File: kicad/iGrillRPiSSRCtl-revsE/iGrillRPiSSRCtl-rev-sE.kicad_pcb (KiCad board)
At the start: 2 copper layers, 65 x 56 mm, 42 parts, among them J1 Screw_Terminal_01x02, P1 Conn_02x20_Odd_Even, Q1 Q_NPN_ECB, Q2 Q_NPN_ECB, Q3 Q_NPN_ECB, Q4 Q_NPN_ECB, Q5 Q_NPN_ECB, Q6 Q_NPN_ECB, Q7 Q_NPN_ECB, Q8 Q_NPN_ECB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

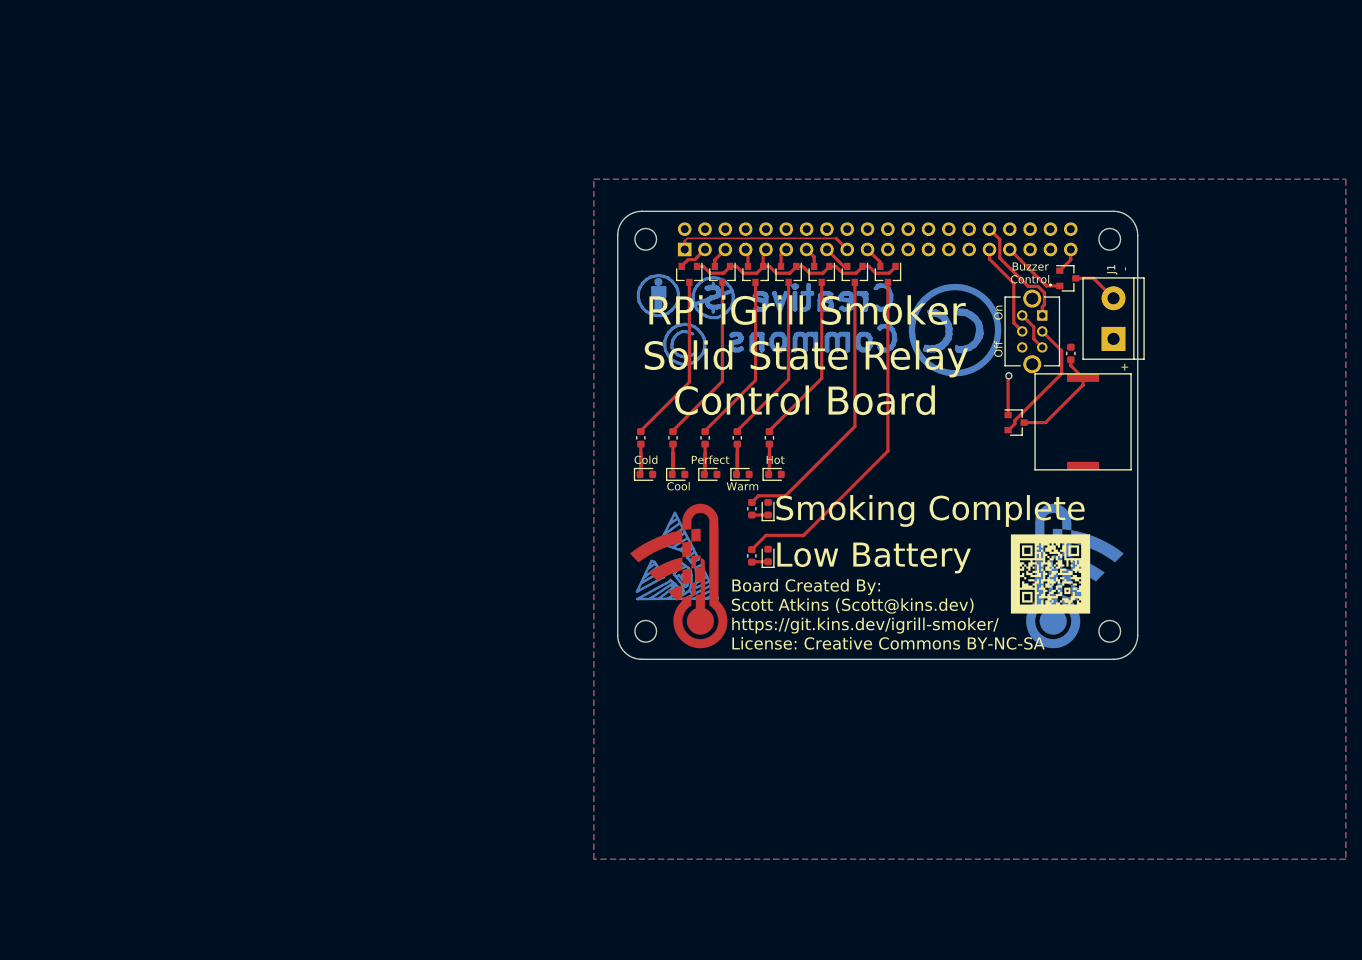
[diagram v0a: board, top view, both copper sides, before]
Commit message: Updating buzzer and design for *e
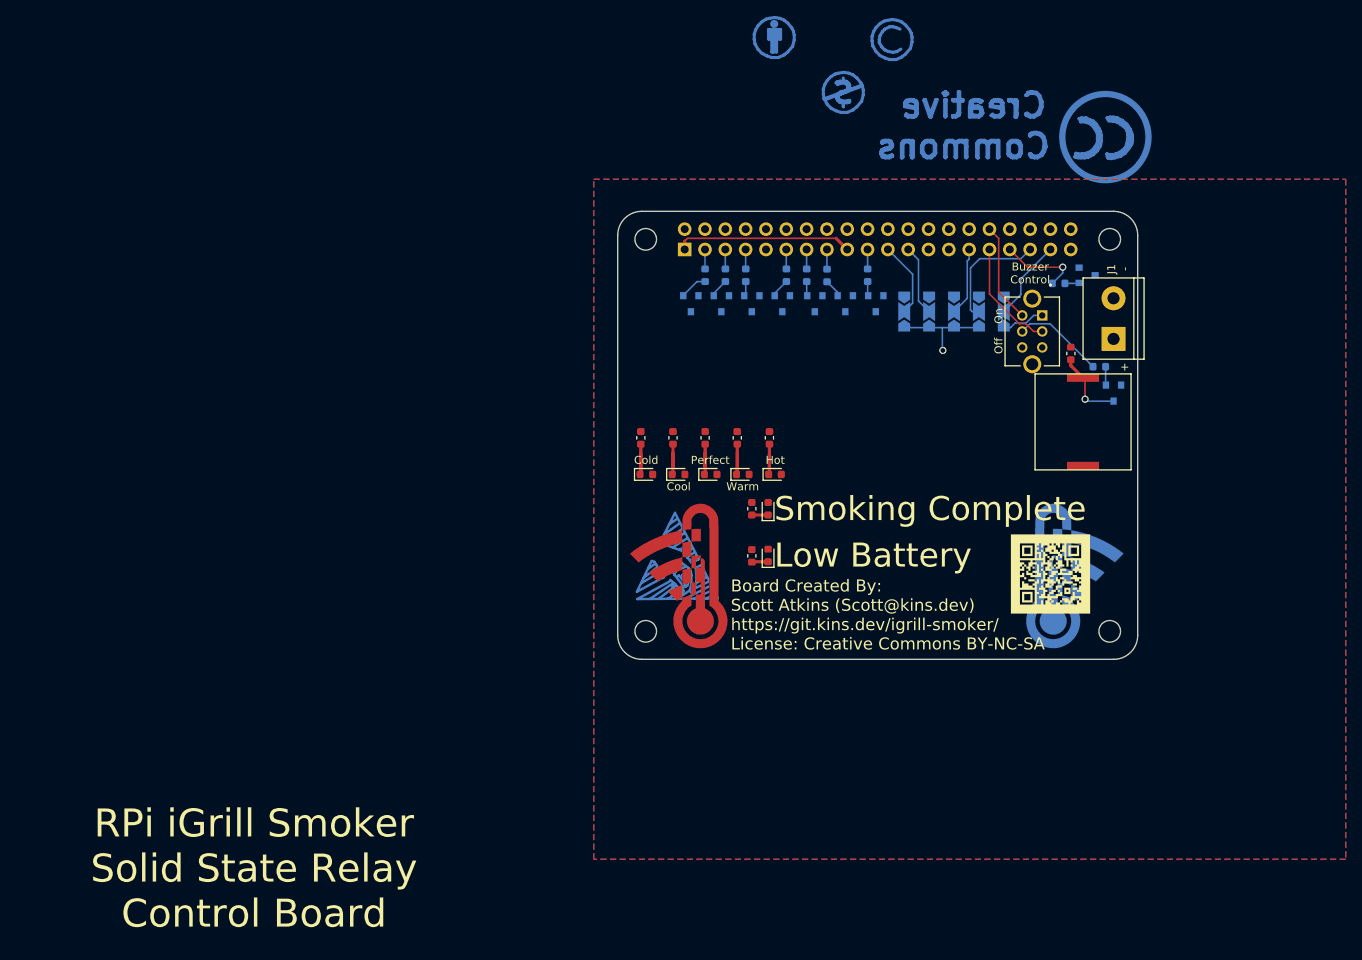
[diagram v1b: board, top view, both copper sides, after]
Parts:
- added JP1: Jumper_3_Open, Jumper:SolderJumper-3_P2.0mm_Open_TrianglePad1.0x1.5mm_NumberLabels, B.Cu at (52.9, 30.3)
- added JP2: Jumper_3_Open, Jumper:SolderJumper-3_P2.0mm_Open_TrianglePad1.0x1.5mm_NumberLabels, B.Cu at (56.0, 30.3)
- added JP3: Jumper_3_Open, Jumper:SolderJumper-3_P2.0mm_Open_TrianglePad1.0x1.5mm_NumberLabels, B.Cu at (59.2, 30.3)
- added JP4: Jumper_3_Open, Jumper:SolderJumper-3_P2.0mm_Open_TrianglePad1.0x1.5mm_NumberLabels, B.Cu at (62.3, 30.3)
- added JP5: Jumper_3_Open, Jumper:SolderJumper-3_P2.0mm_Open_TrianglePad1.0x1.5mm_NumberLabels, B.Cu at (65.4, 30.3)
- added R10: 180Ω, Resistor_SMD:R_0603_1608Metric, B.Cu at (33.1, 25.8)
- added R11: 180Ω, Resistor_SMD:R_0603_1608Metric, B.Cu at (72.2, 26.8)
- added R13: 180Ω, Resistor_SMD:R_0603_1608Metric, B.Cu at (30.6, 25.8)
- added R15: 180Ω, Resistor_SMD:R_0603_1608Metric, B.Cu at (28.0, 25.8)
- added R16: 180Ω, Resistor_SMD:R_0603_1608Metric, B.Cu at (77.3, 37.2)
- added R2: 180Ω, Resistor_SMD:R_0603_1608Metric, B.Cu at (48.4, 25.8)
- added R4: 180Ω, Resistor_SMD:R_0603_1608Metric, B.Cu at (43.3, 25.8)
- added R6: 180Ω, Resistor_SMD:R_0603_1608Metric, B.Cu at (40.7, 25.8)
- added R8: 180Ω, Resistor_SMD:R_0603_1608Metric, B.Cu at (38.2, 25.8)
- Q1, Q2, Q3, Q4, Q5, Q6, Q7, Q8, Q9: value Q_NPN_ECB -> MMBT3904LT1G; moved to B.Cu
- R1, R5: value 120Ω -> 180Ω
- R12: renamed from R8; value 120Ω -> 180Ω
- R14: renamed from R9; value 120Ω -> 180Ω
- R3: renamed from R2; value 82Ω -> 180Ω
- R7: renamed from R6; value 120Ω -> 180Ω
- R9: renamed from R7; value 82Ω -> 180Ω
- SW1: value Off On -> Off On
- moved REF** 46.1 mm to (51.4, -3.67)
- moved Q6 41.4 mm to (75.8, 25.8), turned to 0 degrees
- moved REF** 35.4 mm to (36.7, -3.92)
- moved REF** 30.6 mm to (78.1, 8.52)
- moved REF** 30.4 mm to (45.3, 2.93)
- moved Q1 23.0 mm to (49.4, 29.4), turned to 270 degrees
- moved Q9 15.4 mm to (79.1, 40.5), turned to 270 degrees
- moved Q2 6.47 mm to (45.6, 29.4)
- moved Q3 6.20 mm to (41.8, 29.4)
- moved Q4 6.15 mm to (37.7, 29.4)
- moved Q5 5.88 mm to (33.9, 29.4)
- moved Q8 3.67 mm to (26.3, 29.4)
- moved Q7 3.67 mm to (30.1, 29.4)
- renumbered R4 to R17
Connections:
- P1 pad 10: +5V -> GND
- P1 pad 12: GND -> +5V
- P1 pad 8: +5V -> GND
- Q1 pad 1: GND -> Net-(Q1-Pad1)
- Q1 pad 2: Net-(Q1-Pad2) -> GND
- Q1 pad 3: Net-(BZ1-Pad2) -> Net-(Q1-Pad3)
- Q2 pad 1: GND -> Net-(Q2-Pad1)
- Q2 pad 2: /GPIO10(SPI0_MOSI) -> GND
- Q3 pad 1: GND -> Net-(Q3-Pad1)
- Q3 pad 2: /GPIO22(GEN3) -> GND
- Q4 pad 1: GND -> Net-(Q4-Pad1)
- Q4 pad 2: /GPIO27(GEN2) -> GND
- Q5 pad 1: GND -> Net-(Q5-Pad1)
- Q5 pad 2: /GPIO17(GEN0) -> GND
- Q6 pad 1: GND -> Net-(Q6-Pad1)
- Q6 pad 2: /GPIO4(GCLK) -> GND
- Q6 pad 3: Net-(Q6-Pad3) -> Net-(J1-Pad2)
- Q7 pad 1: GND -> Net-(Q7-Pad1)
- Q7 pad 2: /GPIO3(SCL1) -> GND
- Q8 pad 1: GND -> Net-(Q8-Pad1)
- Q8 pad 2: /GPIO2(SDA1) -> GND
- Q9 pad 1: GND -> Net-(Q9-Pad1)
- Q9 pad 2: /GPIO13(PWM1) -> GND
- Q9 pad 3: Net-(J1-Pad2) -> Net-(BZ1-Pad2)
- R1 pad 2: Net-(Q2-Pad3) -> Net-(Q1-Pad3)
- R3 pad 2: Net-(Q3-Pad3) -> Net-(Q2-Pad3)
- R5 pad 2: Net-(Q4-Pad3) -> Net-(Q3-Pad3)
- R7 pad 2: Net-(Q5-Pad3) -> Net-(Q4-Pad3)
- R9 pad 2: Net-(Q6-Pad3) -> Net-(Q5-Pad3)
- SW1 pad 1: /GPIO12(PWM0) -> +5V
- SW1 pad 2: Net-(Q1-Pad2) -> /GPIO6
- SW1 pad 3: +5V -> GND
- SW1 pad 4: +5V -> /GPIO12(PWM0)
- SW1 pad 5: /GPIO6 -> Net-(R16-Pad1)
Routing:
- net Net-(Q2-Pad3): track 43.2 -> 0.00 mm
- net GND: track 39.6 -> 0.00 mm, vias 1 -> 0
- net Net-(Q3-Pad3): track 34.8 -> 0.00 mm
- net Net-(Q4-Pad3): track 21.3 -> 0.00 mm
- net Net-(Q5-Pad3): track 21.2 -> 0.00 mm
- net Net-(Q6-Pad3): track 21.2 -> 0.00 mm
- net Net-(Q7-Pad3): track 21.1 -> 0.00 mm
- net Net-(Q8-Pad3): track 21.1 -> 0.00 mm
- net Net-(Q1-Pad2): track 16.2 -> 0.00 mm
- net /GPIO19(SPI1_MISO): track 0.00 -> 14.8 mm
- net +5V: track 5.04 -> 17.8 mm, vias 0 -> 1
- net Net-(R16-Pad1): track 0.00 -> 11.5 mm
- net /GPIO26: track 0.00 -> 10.2 mm
- net /GPIO9(SPI0_MISO): track 0.00 -> 9.48 mm
- net /GPIO11(SPI0_SCK): track 0.00 -> 8.85 mm
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
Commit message: *E board updates
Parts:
- G***: footprint iGrillRPiSSRCtl-rev-sE:qr-code-10x10_inverted -> iGrillRPiSSRCtl-rev-sE:github-qr-11.7mm
- G***: footprint iGrillRPiSSRCtl-rev-sE:qr-code-12x12 -> iGrillRPiSSRCtl-rev-sE:github-qr-11.7mm
- moved REF** 58.2 mm to (25.0, 48.1)
- moved REF** 52.1 mm to (39.2, 48.1)
- moved REF** 47.1 mm to (32.1, 48.1)
- moved REF** 44.1 mm to (49.1, 41.8)
- moved D7 41.2 mm to (61.7, 46.4)
- moved D6 29.5 mm to (53.9, 46.4)
- moved G*** 22.1 mm to (40.0, 57.3)
- moved D5 17.8 mm to (46.0, 46.4)
- moved R5 13.4 mm to (23.0, 43.1), turned to 180 degrees
- moved R7 10.2 mm to (22.0, 44.8), turned to 180 degrees
- moved D3 7.76 mm to (30.3, 46.4)
- moved R9 7.11 mm to (21.0, 46.6), turned to 180 degrees
- moved D4 6.93 mm to (38.2, 46.4)
- moved G*** 4.84 mm to (76.0, 62.8)
- moved R12 4.68 mm to (19.9, 48.4), turned to 180 degrees
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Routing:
- net Net-(Q1-Pad3): track 0.00 -> 69.4 mm, vias 0 -> 1
- net Net-(Q2-Pad3): track 0.00 -> 61.7 mm, vias 0 -> 1
- net Net-(D7-Pad1): track 6.39 -> 42.8 mm
- net Net-(Q3-Pad3): track 0.00 -> 29.9 mm, vias 0 -> 1
- net Net-(Q4-Pad3): track 0.00 -> 29.2 mm, vias 0 -> 1
- net Net-(Q5-Pad3): track 0.00 -> 28.8 mm, vias 0 -> 1
- net Net-(Q7-Pad3): track 0.00 -> 28.4 mm, vias 0 -> 1
- net Net-(D6-Pad1): track 5.54 -> 33.5 mm
- net Net-(Q8-Pad3): track 0.00 -> 27.9 mm, vias 0 -> 1
- net Net-(D5-Pad1): track 5.72 -> 25.1 mm
- net Net-(D4-Pad1): track 6.39 -> 17.9 mm
- net Net-(J1-Pad2): track 0.00 -> 3.84 mm
- net Net-(D3-Pad1): track 6.39 -> 10.2 mm
- net +5V: track 17.8 -> 18.1 mm, vias 1 -> 0
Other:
- board text added: "13 - SSR (J1) 10 - Low Battery 22 - Smoking Complete 02 - Cold 03 - Cool 04 - Perfect 17 - Warm 22 - Hot 06 - Switch 12 - Buzzer"
- board text removed: "02 - Cold 03 - Cool 04 - Perfect 17 - Warm 22 - Hot 10 - Low Battery 22 - Smoking Complete 06 - Switch 12 - Buzzer 13 - SSR (J1)"
- board text removed: "Board Created By: Scott Atkins (Scott@kins.dev) https://git.kins.dev/igrill-smoker/"

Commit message: Board Updates
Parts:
- D3: value Hot -> Cold
- D4: value Warm -> Cool
- D6: value Cool -> Warm
- D7: value Cold -> Hot
- moved G*** 3.17 mm to (36.8, 57.3)
- moved REF** 2.79 mm to (48.9, 57.0)
- moved D1 1.78 mm to (35.9, 59.0)
- moved D2 1.78 mm to (35.9, 53.2)
- moved R1 1.78 mm to (33.9, 59.1)
- moved R3 1.78 mm to (33.9, 53.2)
- moved D3 1.40 mm to (30.3, 45.0)
- moved D4 1.40 mm to (38.2, 45.0)
- moved D5 1.40 mm to (46.0, 45.0)
- moved D6 1.40 mm to (53.9, 45.0)
- moved D7 1.40 mm to (61.7, 45.0)
- moved REF** 1.28 mm to (49.3, 40.5)
- moved REF** 1.17 mm to (39.0, 47.0)
- moved REF** 1.17 mm to (24.7, 47.0)
- moved REF** 1.17 mm to (31.9, 47.0)
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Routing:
- net Net-(Q3-Pad3): track 29.9 -> 35.2 mm
- net Net-(D3-Pad1): track 10.2 -> 6.55 mm
- net Net-(Q4-Pad3): track 29.2 -> 31.9 mm
- net Net-(D4-Pad1): track 17.9 -> 15.3 mm
- net Net-(D7-Pad1): track 42.8 -> 45.1 mm
- net Net-(D6-Pad1): track 33.5 -> 35.0 mm
- net Net-(Q5-Pad3): track 28.8 -> 30.2 mm
- net Net-(Q8-Pad3): track 27.9 -> 28.9 mm
- net Net-(Q7-Pad3): track 28.4 -> 29.3 mm
- net +5V: track 18.1 -> 18.9 mm
- net Net-(BZ1-Pad2): track 9.32 -> 8.50 mm
- net Net-(R16-Pad1): track 11.5 -> 10.7 mm
- net Net-(Q2-Pad3): track 61.7 -> 62.5 mm
- net /GPIO11(SPI0_SCK): track 8.85 -> 9.42 mm
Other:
- board text added: "Board By: Scott Atkins Scott@kins.dev"
- board text added: "Serial Number:"
- board text added: "https://git.kins.dev/igrill-smoker/"

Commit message: *E updates
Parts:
- R1, R11, R12, R14, R16, R3, R5, R7, R9: value 180Ω -> 1kΩ
- SW1: value Off On -> SW_SPDT; footprint iGrillRPiSSRCtl-rev-sE:SW_OS202011MS2QS1 -> Button_Switch_THT:SW_Slide_1P2T_CK_OS102011MS2Q
- moved SW1 3.09 mm to (70.8, 30.3)
- moved R11 0.76 mm to (72.2, 26.0)
- moved R17 0.67 mm to (74.2, 35.1)
- moved Q6 0.38 mm to (75.8, 26.2)
- moved R10 0.13 mm to (33.1, 25.9)
- moved R13 0.13 mm to (30.6, 25.9)
- moved R15 0.13 mm to (28.0, 25.9)
- moved R2 0.13 mm to (48.4, 25.9)
- moved R6 0.13 mm to (40.7, 25.9)
- moved R8 0.13 mm to (38.2, 25.9)
- moved R4 0.10 mm to (43.3, 25.9)
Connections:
- R16 pad 1: Net-(R16-Pad1) -> /GPIO6
- SW1 pad 1: +5V -> /GPIO12(PWM0)
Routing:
- net Net-(R16-Pad1): track 10.7 -> 0.00 mm
- net +5V: track 18.9 -> 27.5 mm, vias 0 -> 1
- net /GPIO6: track 14.1 -> 21.5 mm
- net Net-(J1-Pad2): track 3.84 -> 7.29 mm
- net Net-(Q8-Pad1): track 3.49 -> 6.90 mm
- net /GPIO26: track 10.2 -> 13.1 mm
- net Net-(Q1-Pad3): track 69.5 -> 72.3 mm
- net /GPIO4(GCLK): track 2.44 -> 5.01 mm
- net /GPIO3(SCL1): track 2.44 -> 5.01 mm
- net /GPIO27(GEN2): track 2.44 -> 5.01 mm
- net /GPIO2(SDA1): track 2.44 -> 5.01 mm
- net /GPIO17(GEN0): track 2.44 -> 5.01 mm
- net /GPIO10(SPI0_MOSI): track 2.44 -> 5.01 mm
- net /GPIO22(GEN3): track 2.76 -> 5.33 mm
- net Net-(Q3-Pad3): track 35.2 -> 37.6 mm
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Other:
- board text added: "26 - ID0 19 - ID1 05 - ID2 11 - ID3 09 - ID4 13 - SSR (J1) 10 - Low Battery 22 - Smoking Complete 02 - Cold 03 - Cool 04 - Perfect 17 - Warm 22 - Hot 06 - Switch 12 - Buzzer"
- board text added: "Buzzer"
- board text removed: "13 - SSR (J1) 10 - Low Battery 22 - Smoking Complete 02 - Cold 03 - Cool 04 - Perfect 17 - Warm 22 - Hot 06 - Switch 12 - Buzzer"
- board text removed: "Buzzer Control"

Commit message: Fixing pulldown resistors
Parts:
- added R18: 10kΩ, Resistor_SMD:R_0603_1608Metric, B.Cu at (50.1, 26.0)
- added R19: 10kΩ, Resistor_SMD:R_0603_1608Metric, B.Cu at (46.3, 26.0)
- added R20: 10kΩ, Resistor_SMD:R_0603_1608Metric, B.Cu at (42.5, 26.0)
- added R21: 10kΩ, Resistor_SMD:R_0603_1608Metric, B.Cu at (38.7, 26.0)
- added R22: 10kΩ, Resistor_SMD:R_0603_1608Metric, B.Cu at (74.5, 29.6)
- added R23: 10kΩ, Resistor_SMD:R_0603_1608Metric, B.Cu at (34.8, 26.0)
- added R24: 10kΩ, Resistor_SMD:R_0603_1608Metric, B.Cu at (31.0, 26.0)
- added R25: 10kΩ, Resistor_SMD:R_0603_1608Metric, B.Cu at (27.2, 26.0)
- added R26: 10kΩ, Resistor_SMD:R_0603_1608Metric, B.Cu at (74.5, 32.7)
- R1, R12, R14, R3, R5, R7, R9: value 1kΩ -> 180Ω
- R10, R13, R15, R2, R4, R6, R8: value 180Ω -> 1kΩ
- moved R15 2.80 mm to (25.2, 26.0)
- moved R13 1.51 mm to (29.1, 26.0)
- moved R8 1.47 mm to (36.7, 26.0)
- moved R4 1.12 mm to (44.4, 26.0)
- moved R10 0.24 mm to (32.9, 26.0)
- moved R6 0.20 mm to (40.6, 26.0)
- moved R2 0.17 mm to (48.2, 26.0)
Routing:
- net Net-(Q8-Pad1): track 6.90 -> 1.62 mm
- net GND: track 0.00 -> 3.26 mm
- net Net-(Q4-Pad1): track 4.62 -> 1.54 mm
- net Net-(Q7-Pad1): track 4.62 -> 1.56 mm
- net Net-(Q2-Pad1): track 4.49 -> 1.63 mm
- net /GPIO6: track 21.5 -> 23.6 mm
- net Net-(Q6-Pad1): track 2.14 -> 3.94 mm
- net Net-(Q1-Pad1): track 3.37 -> 1.62 mm
- net Net-(Q3-Pad1): track 3.37 -> 1.64 mm
- net Net-(Q5-Pad1): track 3.30 -> 1.82 mm
- net +3V3: track 22.1 -> 21.4 mm
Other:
- board text added: "26 - ID0 19 - ID1 05 - ID2 11 - ID3 09 - ID4 13 - SSR (J1) 10 - Low Battery 22 - Smoking Complete 27 - Cold 17 - Cool 04 - Perfect 03 - Warm 02 - Hot 06 - Switch 12 - Buzzer"
- board text removed: "26 - ID0 19 - ID1 05 - ID2 11 - ID3 09 - ID4 13 - SSR (J1) 10 - Low Battery 22 - Smoking Complete 02 - Cold 03 - Cool 04 - Perfect 17 - Warm 22 - Hot 06 - Switch 12 - Buzzer"
